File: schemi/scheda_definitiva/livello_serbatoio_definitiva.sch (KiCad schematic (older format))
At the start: 36 parts, among them J1 USB_B, J2 BTN_LED_GROUP, J3 CONN_LCD, J4 CONN_US, J5 ICSP, SW1 SW_RST, U1 FT232RL, U2 ATmega328P-PU, Y1 16MHz

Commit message: aggiunta protezione ESD - nuovo routing usb - nuove immagini pcb
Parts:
- added C5: 100nF, Capacitor_THT:C_Disc_D5.0mm_W2.5mm_P2.50mm, symbol Device:C
- added U3: USBLC6-2SC6, Package_TO_SOT_SMD:SOT-23-6_Handsoldering, symbol Power_Protection:USBLC6-2SC6
- D3: value 1N4148TR -> 1N4700; footprint Diode_THT:D_DO-35_SOD27_P7.62mm_Horizontal -> Diode_THT:D_DO-41_SOD81_P7.62mm_Horizontal
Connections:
- net labels added: D_IN_+, D_IN_-, D_OUT_+, D_OUT_-, VBUS
- net labels removed: D+, D-
- wire segments 161 -> 163
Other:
- note added: "ESD Protection"
- moved on the sheet: C1, C4, D3, R5, R6, SW1

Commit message: allineamento modello 3d + fix minori pcb - aggiornato modello box - aggiunto logo a box - nuovi modelli 3d fusibile e trimmer - aggiornato sch per fusibile - aggiornato pcb - nuove immagini + doc prototipo pdf
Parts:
- removed FB1: MF-MSMF050-2, Inductor_SMD:L_1812_4532Metric_Pad1.30x3.40mm_HandSolder, symbol Device:Ferrite_Bead
- added F1: MF-MSMF050-2, simboli_custom:MF-MSMF_1812_4532Metric_Pad1.30x3.40mm_HandSolder, symbol Device:Polyfuse
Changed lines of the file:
@@
 	1    0    0    -1
-$EndComp
-$Comp
-L Device:Ferrite_Bead FB1
-U 1 1 5F8E145F
-P 1500 2350
-F 0 "FB1" V 1350 2350 50  0000 C CNN
-F 1 "MF-MSMF050-2" V 1650 2500 50  0000 C CNN
-F 2 "Inductor_SMD:L_1812_4532Metric_Pad1.30x3.40mm_HandSolder" V 1430 2350 50  0001 C CNN
-F 3 "~" H 1500 2350 50  0001 C CNN
-	1    1500 2350
-	0    1    1    0
 $EndComp
 Text Label 1700 4350 0    50   ~ 0
@@
 	3050 2350 2950 2350
 $Comp
-L power:GND #PWR?
+L power:GND #PWR0104
 U 1 1 5FD135C3
 P 3050 2000
-F 0 "#PWR?" H 3050 1750 50  0001 C CNN
+F 0 "#PWR0104" H 3050 1750 50  0001 C CNN
 F 1 "GND" V 3055 1872 50  0000 R CNN
 F 2 "" H 3050 2000 50  0001 C CNN
@@
 	0    -1   -1   0
 $EndComp
+$Comp
+L Device:Polyfuse F1
+U 1 1 5FB200DA
+P 1500 2350
+F 0 "F1" V 1400 2350 50  0000 C CNN
+F 1 "MF-MSMF050-2" V 1600 2500 50  0000 C CNN
+F 2 "simboli_custom:MF-MSMF_1812_4532Metric_Pad1.30x3.40mm_HandSolder" H 1550 2150 50  0001 L CNN
+F 3 "~" H 1500 2350 50  0001 C CNN
+	1    1500 2350
+	0    1    1    0
+$EndComp
 $EndSCHEMATC

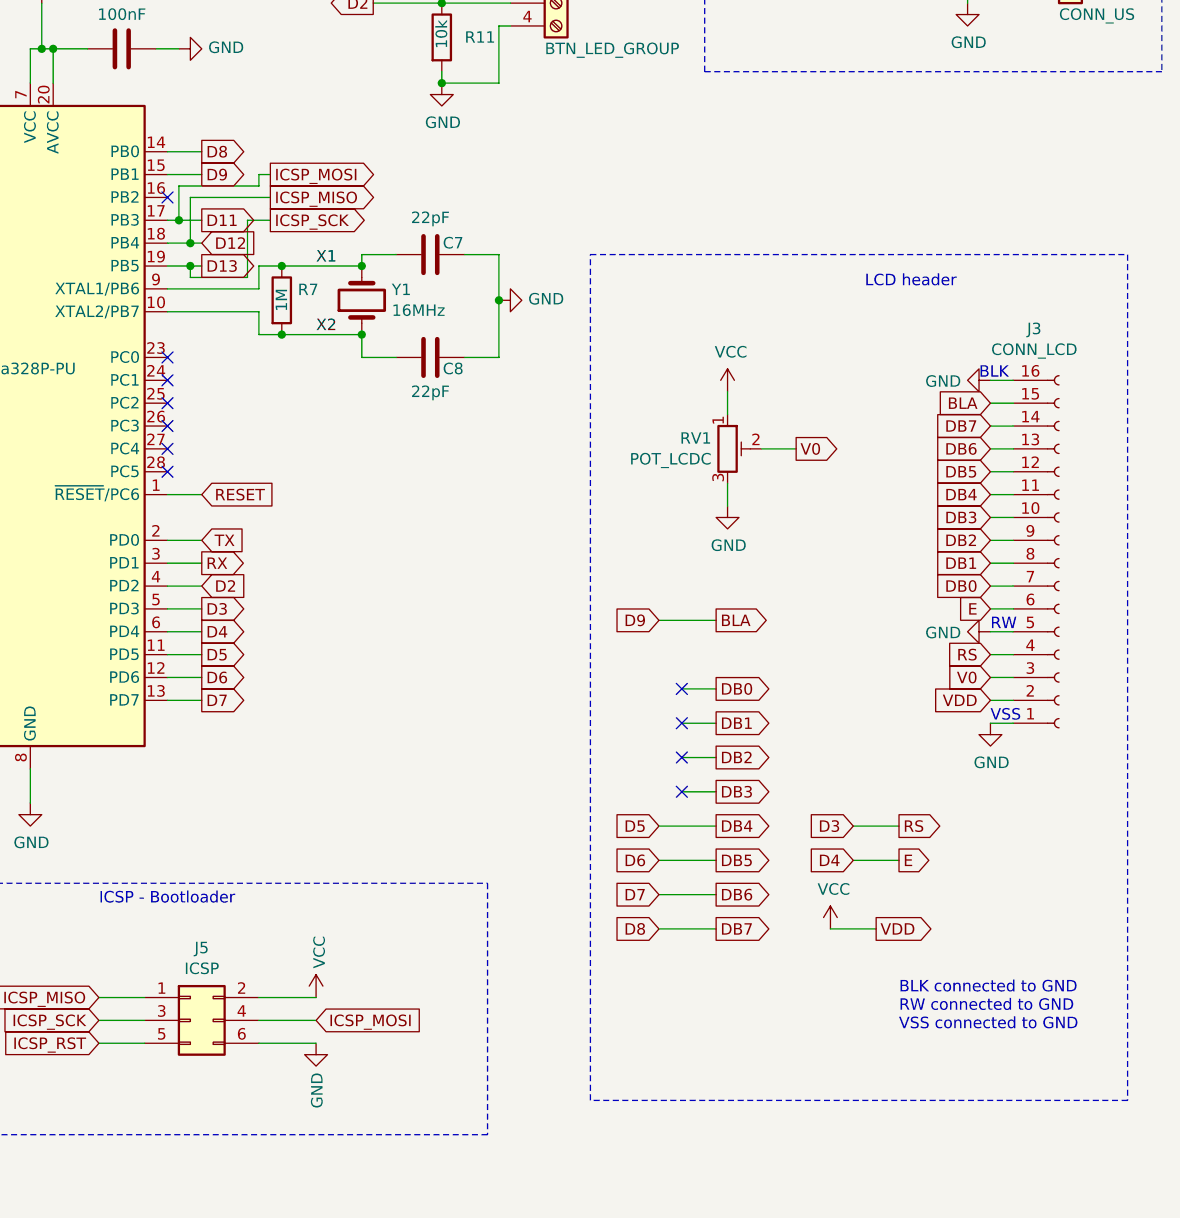
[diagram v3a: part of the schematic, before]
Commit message: esportati pin per espandibilità
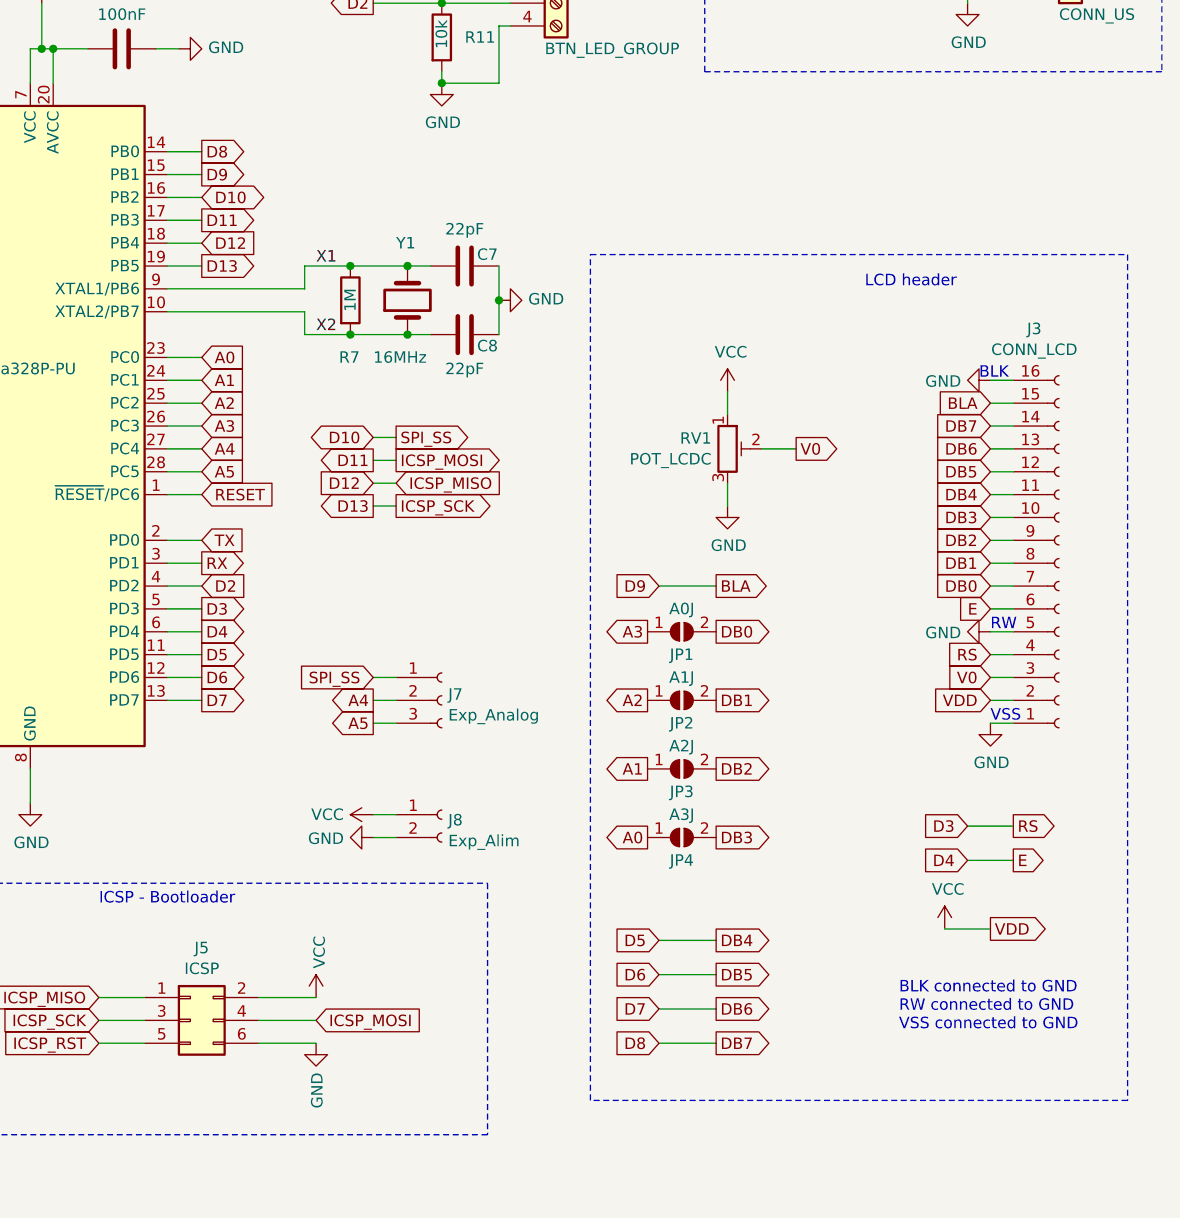
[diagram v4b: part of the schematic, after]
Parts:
- added J7: Exp_Analog, Connector_PinSocket_2.54mm:PinSocket_1x03_P2.54mm_Vertical, symbol Connector:Conn_01x03_Female
- added J8: Exp_Alim, Connector_PinSocket_2.54mm:PinSocket_1x02_P2.54mm_Vertical, symbol Connector:Conn_01x02_Female
- added JP1: A0J, Jumper:SolderJumper-2_P1.3mm_Open_Pad1.0x1.5mm, symbol Jumper:SolderJumper_2_Open
- added JP2: A1J, Jumper:SolderJumper-2_P1.3mm_Open_Pad1.0x1.5mm, symbol Jumper:SolderJumper_2_Open
- added JP3: A2J, Jumper:SolderJumper-2_P1.3mm_Open_Pad1.0x1.5mm, symbol Jumper:SolderJumper_2_Open
- added JP4: A3J, Jumper:SolderJumper-2_P1.3mm_Open_Pad1.0x1.5mm, symbol Jumper:SolderJumper_2_Open
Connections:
- net DB0: now also JP1.2 (B)
- net DB1: now also JP2.2 (B)
- net DB2: now also JP3.2 (B)
- net DB3: now also JP4.2 (B)
- net GND: now also J8.2 (Pin_2)
- net VCC: now also J8.1 (Pin_1)
- net D10: now reaches U2.16 (PB2)
- net D10: now also J7.1 (Pin_1)
- net A0: now reaches U2.23 (PC0)
- net A0: now also JP4.1 (A)
- net A1: now reaches U2.24 (PC1)
- net A1: now also JP3.1 (A)
- net A2: now reaches U2.25 (PC2)
- net A2: now also JP2.1 (A)
- net A3: now reaches U2.26 (PC3)
- net A3: now also JP1.1 (A)
- net A4: now reaches U2.27 (PC4)
- net A4: now also J7.2 (Pin_2)
- net A5: now reaches U2.28 (PC5)
- net A5: now also J7.3 (Pin_3)
- no-connect marks 21 -> 10
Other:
- moved on the sheet: C7, C8, R7, Y1

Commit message: aggiornamento PCB - ridefinite filled zone - stondati bordi - cambiato connettore per espansione - rimosse via per GND
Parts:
- removed J8: Exp_Alim, Connector_PinSocket_2.54mm:PinSocket_1x02_P2.54mm_Vertical, symbol Connector:Conn_01x02_Female
- J7: footprint Connector_PinSocket_2.54mm:PinSocket_1x03_P2.54mm_Vertical -> Connector_PinSocket_2.54mm:PinSocket_1x05_P2.54mm_Vertical; symbol Connector:Conn_01x03_Female -> Connector:Conn_01x05_Female
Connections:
- net A4: now also J7.4 (Pin_4); no longer J7.2 (Pin_2)
- net A5: now also J7.5 (Pin_5); no longer J7.3 (Pin_3)
- net D10: now also J7.3 (Pin_3); no longer J7.1 (Pin_1)
- net GND: now also J7.2 (Pin_2)
- net VCC: now also J7.1 (Pin_1)
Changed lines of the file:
@@
 Text GLabel 8750 4250 0    50   Output ~ 0
 A3
-Text GLabel 7550 4550 0    50   Output ~ 0
+Text GLabel 7550 4650 0    50   Output ~ 0
 A4
-Text GLabel 7550 4650 0    50   Output ~ 0
+Text GLabel 7550 4750 0    50   Output ~ 0
 A5
 $Comp
-L Connector:Conn_01x03_Female J7
+L Connector:Conn_01x05_Female J7
 U 1 1 5FD28169
 P 7850 4550
 F 0 "J7" H 7878 4576 50  0000 L CNN
 F 1 "Exp_Analog" H 7878 4485 50  0000 L CNN
-F 2 "Connector_PinSocket_2.54mm:PinSocket_1x03_P2.54mm_Vertical" H 7850 4550 50  0001 C CNN
+F 2 "Connector_PinSocket_2.54mm:PinSocket_1x05_P2.54mm_Vertical" H 7850 4550 50  0001 C CNN
 F 3 "~" H 7850 4550 50  0001 C CNN
 	1    7850 4550
@@
 $EndComp
 $Comp
-L Connector:Conn_01x02_Female J8
-U 1 1 5FD3EC73
-P 7850 5050
-F 0 "J8" H 7878 5026 50  0000 L CNN
-F 1 "Exp_Alim" H 7878 4935 50  0000 L CNN
-F 2 "Connector_PinSocket_2.54mm:PinSocket_1x02_P2.54mm_Vertical" H 7850 5050 50  0001 C CNN
-F 3 "~" H 7850 5050 50  0001 C CNN
-	1    7850 5050
-	1    0    0    -1
-$EndComp
-$Comp
 L power:GND #PWR0105
 U 1 1 5FD3FBF6
-P 7550 5150
-F 0 "#PWR0105" H 7550 4900 50  0001 C CNN
-F 1 "GND" V 7555 5022 50  0000 R CNN
-F 2 "" H 7550 5150 50  0001 C CNN
-F 3 "" H 7550 5150 50  0001 C CNN
-	1    7550 5150
+P 7550 4450
+F 0 "#PWR0105" H 7550 4200 50  0001 C CNN
+F 1 "GND" V 7555 4322 50  0000 R CNN
+F 2 "" H 7550 4450 50  0001 C CNN
+F 3 "" H 7550 4450 50  0001 C CNN
+	1    7550 4450
 	0    1    1    0
 $EndComp
@@
 L power:VCC #PWR0106
 U 1 1 5FD4360A
-P 7550 5050
-F 0 "#PWR0106" H 7550 4900 50  0001 C CNN
-F 1 "VCC" V 7550 5250 50  0000 C CNN
-F 2 "" H 7550 5050 50  0001 C CNN
-F 3 "" H 7550 5050 50  0001 C CNN
-	1    7550 5050
+P 7550 4350
+F 0 "#PWR0106" H 7550 4200 50  0001 C CNN
+F 1 "VCC" V 7550 4550 50  0000 C CNN
+F 2 "" H 7550 4350 50  0001 C CNN
+F 3 "" H 7550 4350 50  0001 C CNN
+	1    7550 4350
 	0    -1   -1   0
 $EndComp
 Wire Wire Line
-	7550 5050 7650 5050
-Wire Wire Line
-	7550 5150 7650 5150
+	7550 4350 7650 4350
 Wire Wire Line
 	7550 4450 7650 4450
@@
 Wire Wire Line
 	7550 4650 7650 4650
-Text GLabel 7550 4450 0    50   Input ~ 0
+Wire Wire Line
+	7550 4750 7650 4750
+Text GLabel 7550 4550 0    50   Input ~ 0
 SPI_SS
 Text GLabel 8750 5150 0    50   Output ~ 0

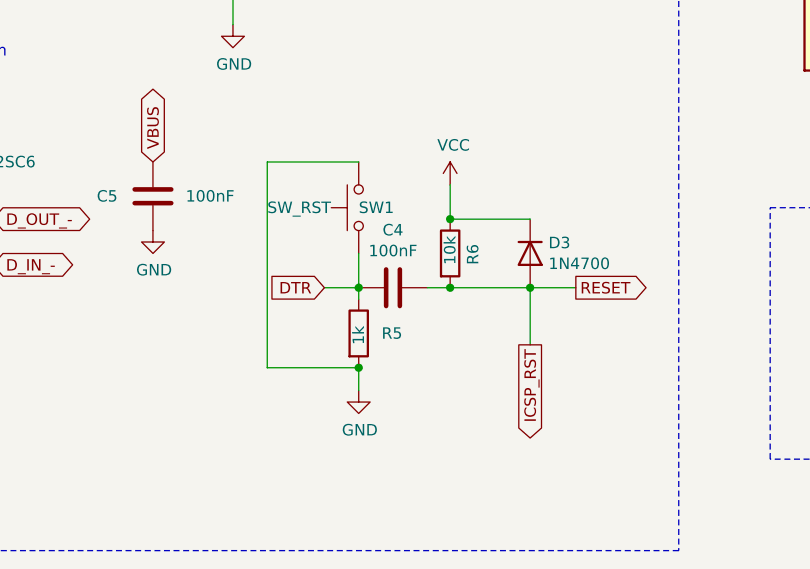
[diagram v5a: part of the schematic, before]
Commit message: revisionata connessione DTR logica reset - revisionato wiring DTR - aggiornato PCB - ricreato gerber
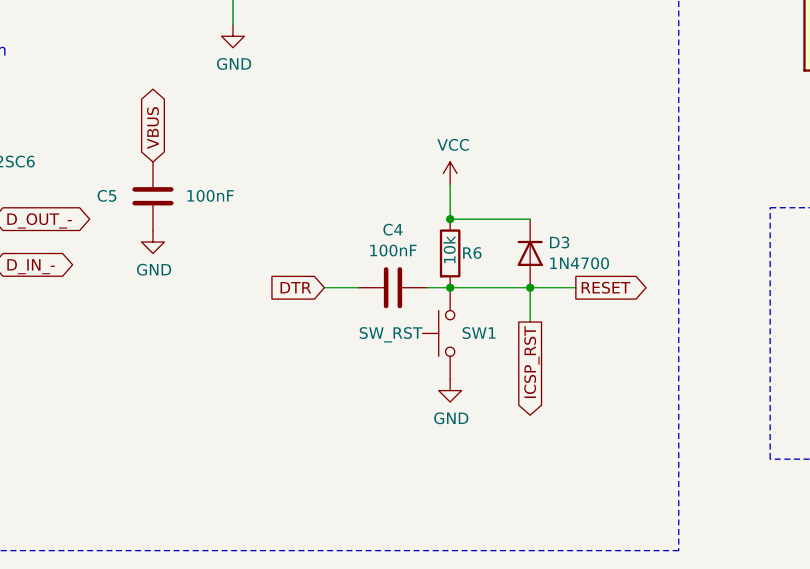
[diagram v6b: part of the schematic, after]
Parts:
- removed R5: 1k, Resistor_THT:R_Axial_DIN0309_L9.0mm_D3.2mm_P12.70mm_Horizontal, symbol Device:R
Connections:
- net DTR: no longer SW1.1
- net GND: now also SW1.1; no longer SW1.2
- net ICSP_RST: now also SW1.2
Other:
- moved on the sheet: SW1
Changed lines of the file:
@@
 U 1 1 5F204DE3
 P 4000 5550
-F 0 "R6" V 4100 5500 50  0000 L CNN
+F 0 "R6" H 4050 5550 50  0000 L CNN
 F 1 "10k" V 4000 5500 50  0000 L CNN
 F 2 "Resistor_THT:R_Axial_DIN0309_L9.0mm_D3.2mm_P12.70mm_Horizontal" V 3930 5550 50  0001 C CNN
@@
 DTR
 $Comp
-L Device:C C4
-U 1 1 5F23FB6A
-P 3750 5700
-F 0 "C4" V 3498 5700 50  0000 C CNN
-F 1 "100nF" V 3589 5700 50  0000 C CNN
-F 2 "Capacitor_THT:C_Disc_D5.0mm_W2.5mm_P2.50mm" H 3788 5550 50  0001 C CNN
-F 3 "~" H 3750 5700 50  0001 C CNN
-	1    3750 5700
-	0    1    1    0
-$EndComp
-$Comp
-L Device:R R5
-U 1 1 5F24028B
-P 3600 5900
-F 0 "R5" H 3700 5900 50  0000 L CNN
-F 1 "1k" V 3600 5850 50  0000 L CNN
-F 2 "Resistor_THT:R_Axial_DIN0309_L9.0mm_D3.2mm_P12.70mm_Horizontal" V 3530 5900 50  0001 C CNN
-F 3 "~" H 3600 5900 50  0001 C CNN
-	1    3600 5900
-	1    0    0    -1
-$EndComp
-$Comp
 L power:GND #PWR04
 U 1 1 5F2407AF
-P 3600 6150
-F 0 "#PWR04" H 3600 5900 50  0001 C CNN
-F 1 "GND" H 3605 5977 50  0000 C CNN
-F 2 "" H 3600 6150 50  0001 C CNN
-F 3 "" H 3600 6150 50  0001 C CNN
-	1    3600 6150
+P 4000 6100
+F 0 "#PWR04" H 4000 5850 50  0001 C CNN
+F 1 "GND" H 4005 5927 50  0000 C CNN
+F 2 "" H 4000 6100 50  0001 C CNN
+F 3 "" H 4000 6100 50  0001 C CNN
+	1    4000 6100
 	1    0    0    -1
 $EndComp
@@
 	3900 5700 4000 5700
 Connection ~ 4000 5700
-Wire Wire Line
-	3600 5750 3600 5700
-Connection ~ 3600 5700
-Wire Wire Line
-	3600 6050 3600 6150
-$Comp
-L Switch:SW_Push SW1
-U 1 1 5F27E84B
-P 3600 5350
-F 0 "SW1" V 3600 5350 50  0000 R CNN
-F 1 "SW_RST" V 3600 5750 50  0000 R CNN
-F 2 "Button_Switch_THT:SW_PUSH_6mm_H5mm" H 3600 5550 50  0001 C CNN
-F 3 "~" H 3600 5550 50  0001 C CNN
-	1    3600 5350
-	0    -1   -1   0
-$EndComp
-Wire Wire Line
-	3600 5550 3600 5700
-Wire Wire Line
-	3600 5150 3200 5150
-Wire Wire Line
-	3200 5150 3200 6050
-Wire Wire Line
-	3200 6050 3600 6050
-Connection ~ 3600 6050
 $Comp
 L Device:C C3
@@
 Text GLabel 7650 3500 2    50   Output ~ 0
 ICSP_MOSI
-Text GLabel 4350 5950 3    50   Output ~ 0
+Text GLabel 4350 5850 3    50   Output ~ 0
 ICSP_RST
-Wire Wire Line
-	4350 5700 4350 5950
 $Comp
 L Mechanical:MountingHole_Pad H1
@@
 	1    0    0    -1
 $EndComp
+$Comp
+L Switch:SW_Push SW1
+U 1 1 5F27E84B
+P 4000 5900
+F 0 "SW1" V 4000 5850 50  0000 R CNN
+F 1 "SW_RST" V 4000 6300 50  0000 R CNN
+F 2 "Button_Switch_THT:SW_PUSH_6mm_H5mm" H 4000 6100 50  0001 C CNN
+F 3 "~" H 4000 6100 50  0001 C CNN
+	1    4000 5900
+	0    -1   -1   0
+$EndComp
+$Comp
+L Device:C C4
+U 1 1 5F23FB6A
+P 3750 5700
+F 0 "C4" V 3498 5700 50  0000 C CNN
+F 1 "100nF" V 3589 5700 50  0000 C CNN
+F 2 "Capacitor_THT:C_Disc_D5.0mm_W2.5mm_P2.50mm" H 3788 5550 50  0001 C CNN
+F 3 "~" H 3750 5700 50  0001 C CNN
+	1    3750 5700
+	0    1    1    0
+$EndComp
+Wire Wire Line
+	4350 5850 4350 5700
 $EndSCHEMATC

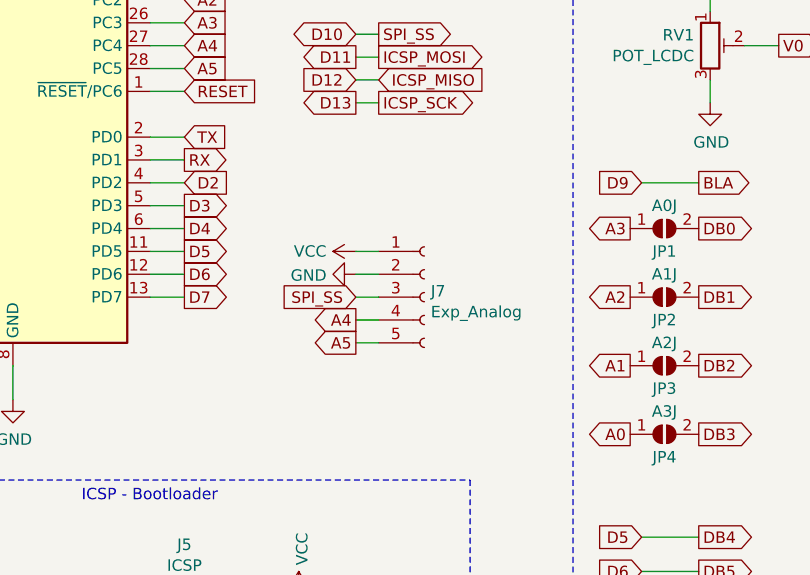
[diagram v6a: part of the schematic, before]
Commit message: aggiunto ulteriore connettore per espansioni - riviste piste - rivisti piani di massa
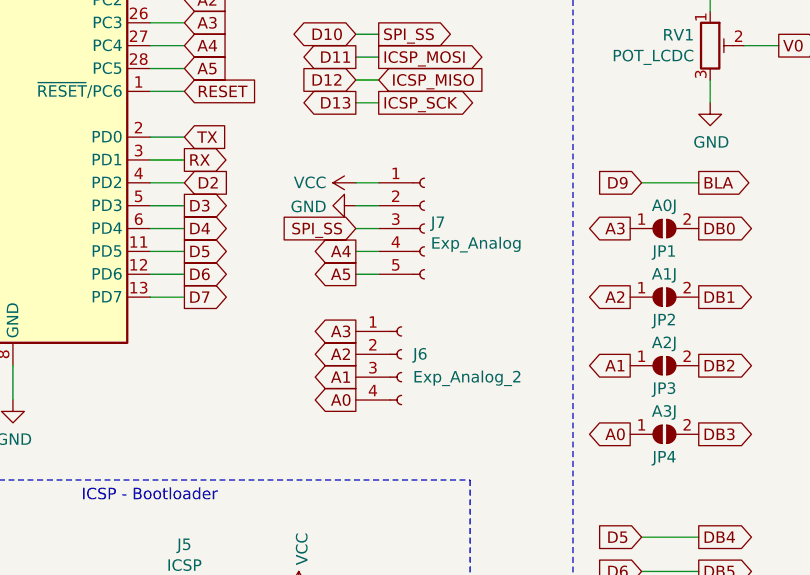
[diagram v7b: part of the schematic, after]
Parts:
- added J6: Exp_Analog_2, Connector_PinSocket_2.54mm:PinSocket_1x04_P2.54mm_Vertical, symbol Connector:Conn_01x04_Female
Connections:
- net A0: now also J6.4 (Pin_4)
- net A1: now also J6.3 (Pin_3)
- net A2: now also J6.2 (Pin_2)
- net A3: now also J6.1 (Pin_1)
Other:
- moved on the sheet: J7
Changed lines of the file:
@@
 Text GLabel 8750 4250 0    50   Output ~ 0
 A3
-Text GLabel 7550 4650 0    50   Output ~ 0
+Text GLabel 7550 4350 0    50   Output ~ 0
 A4
-Text GLabel 7550 4750 0    50   Output ~ 0
+Text GLabel 7550 4450 0    50   Output ~ 0
 A5
 $Comp
 L Connector:Conn_01x05_Female J7
 U 1 1 5FD28169
-P 7850 4550
-F 0 "J7" H 7878 4576 50  0000 L CNN
-F 1 "Exp_Analog" H 7878 4485 50  0000 L CNN
-F 2 "Connector_PinSocket_2.54mm:PinSocket_1x05_P2.54mm_Vertical" H 7850 4550 50  0001 C CNN
-F 3 "~" H 7850 4550 50  0001 C CNN
-	1    7850 4550
+P 7850 4250
+F 0 "J7" H 7878 4276 50  0000 L CNN
+F 1 "Exp_Analog" H 7878 4185 50  0000 L CNN
+F 2 "Connector_PinSocket_2.54mm:PinSocket_1x05_P2.54mm_Vertical" H 7850 4250 50  0001 C CNN
+F 3 "~" H 7850 4250 50  0001 C CNN
+	1    7850 4250
 	1    0    0    -1
 $EndComp
@@
 L power:GND #PWR0105
 U 1 1 5FD3FBF6
-P 7550 4450
-F 0 "#PWR0105" H 7550 4200 50  0001 C CNN
-F 1 "GND" V 7555 4322 50  0000 R CNN
-F 2 "" H 7550 4450 50  0001 C CNN
-F 3 "" H 7550 4450 50  0001 C CNN
-	1    7550 4450
+P 7550 4150
+F 0 "#PWR0105" H 7550 3900 50  0001 C CNN
+F 1 "GND" V 7555 4022 50  0000 R CNN
+F 2 "" H 7550 4150 50  0001 C CNN
+F 3 "" H 7550 4150 50  0001 C CNN
+	1    7550 4150
 	0    1    1    0
 $EndComp
@@
 L power:VCC #PWR0106
 U 1 1 5FD4360A
-P 7550 4350
-F 0 "#PWR0106" H 7550 4200 50  0001 C CNN
-F 1 "VCC" V 7550 4550 50  0000 C CNN
-F 2 "" H 7550 4350 50  0001 C CNN
-F 3 "" H 7550 4350 50  0001 C CNN
-	1    7550 4350
+P 7550 4050
+F 0 "#PWR0106" H 7550 3900 50  0001 C CNN
+F 1 "VCC" V 7550 4250 50  0000 C CNN
+F 2 "" H 7550 4050 50  0001 C CNN
+F 3 "" H 7550 4050 50  0001 C CNN
+	1    7550 4050
 	0    -1   -1   0
 $EndComp
+Wire Wire Line
+	7550 4050 7650 4050
+Wire Wire Line
+	7550 4150 7650 4150
+Wire Wire Line
+	7550 4250 7650 4250
 Wire Wire Line
 	7550 4350 7650 4350
 Wire Wire Line
 	7550 4450 7650 4450
-Wire Wire Line
-	7550 4550 7650 4550
-Wire Wire Line
-	7550 4650 7650 4650
-Wire Wire Line
-	7550 4750 7650 4750
-Text GLabel 7550 4550 0    50   Input ~ 0
+Text GLabel 7550 4250 0    50   Input ~ 0
 SPI_SS
 Text GLabel 8750 5150 0    50   Output ~ 0
@@
 Wire Wire Line
 	4350 5850 4350 5700
+$Comp
+L Connector:Conn_01x04_Female J6
+U 1 1 5FCB4005
+P 7750 4800
+F 0 "J6" H 7800 4800 50  0000 L CNN
+F 1 "Exp_Analog_2" H 7800 4700 50  0000 L CNN
+F 2 "Connector_PinSocket_2.54mm:PinSocket_1x04_P2.54mm_Vertical" H 7750 4800 50  0001 C CNN
+F 3 "~" H 7750 4800 50  0001 C CNN
+	1    7750 4800
+	1    0    0    -1
+$EndComp
+Text GLabel 7550 4700 0    50   Output ~ 0
+A3
+Text GLabel 7550 4800 0    50   Output ~ 0
+A2
+Text GLabel 7550 4900 0    50   Output ~ 0
+A1
+Text GLabel 7550 5000 0    50   Output ~ 0
+A0
 $EndSCHEMATC
